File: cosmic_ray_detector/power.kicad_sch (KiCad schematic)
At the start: 16 parts, among them U2 TPS7A30, U3 TPS7A49

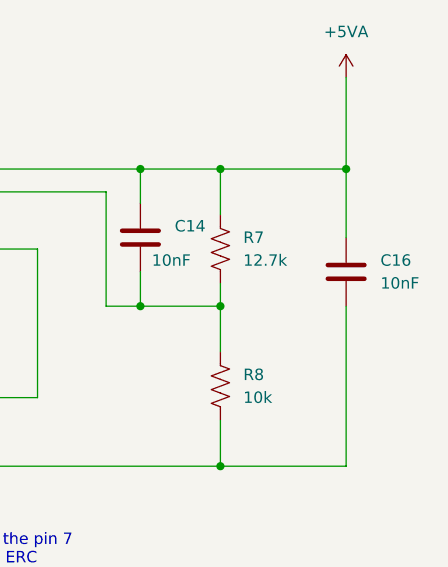
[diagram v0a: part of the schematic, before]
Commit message: change capacitor footprint, place and add zones for +- LDO regs
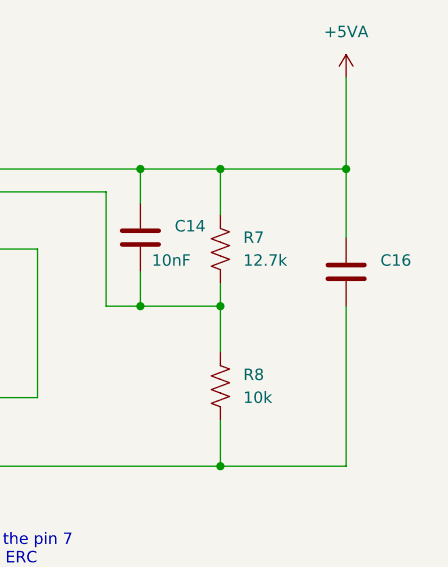
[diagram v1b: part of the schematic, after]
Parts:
- C16: value 10nF -> (none); footprint Capacitor_SMD:C_0402_1005Metric -> (none)
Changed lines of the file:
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@@
       (effects (font (size 1.27 1.27)) (justify left))
     )
-    (property "Value" "10nF" (id 1) (at 180.34 137.1599 0)
+    (property "Value" "" (id 1) (at 180.34 137.1599 0)
       (effects (font (size 1.27 1.27)) (justify left))
     )
-    (property "Footprint" "Capacitor_SMD:C_0402_1005Metric" (id 2) (at 177.4952 139.7 0)
+    (property "Footprint" "" (id 2) (at 177.4952 139.7 0)
       (effects (font (size 1.27 1.27)) hide)
     )

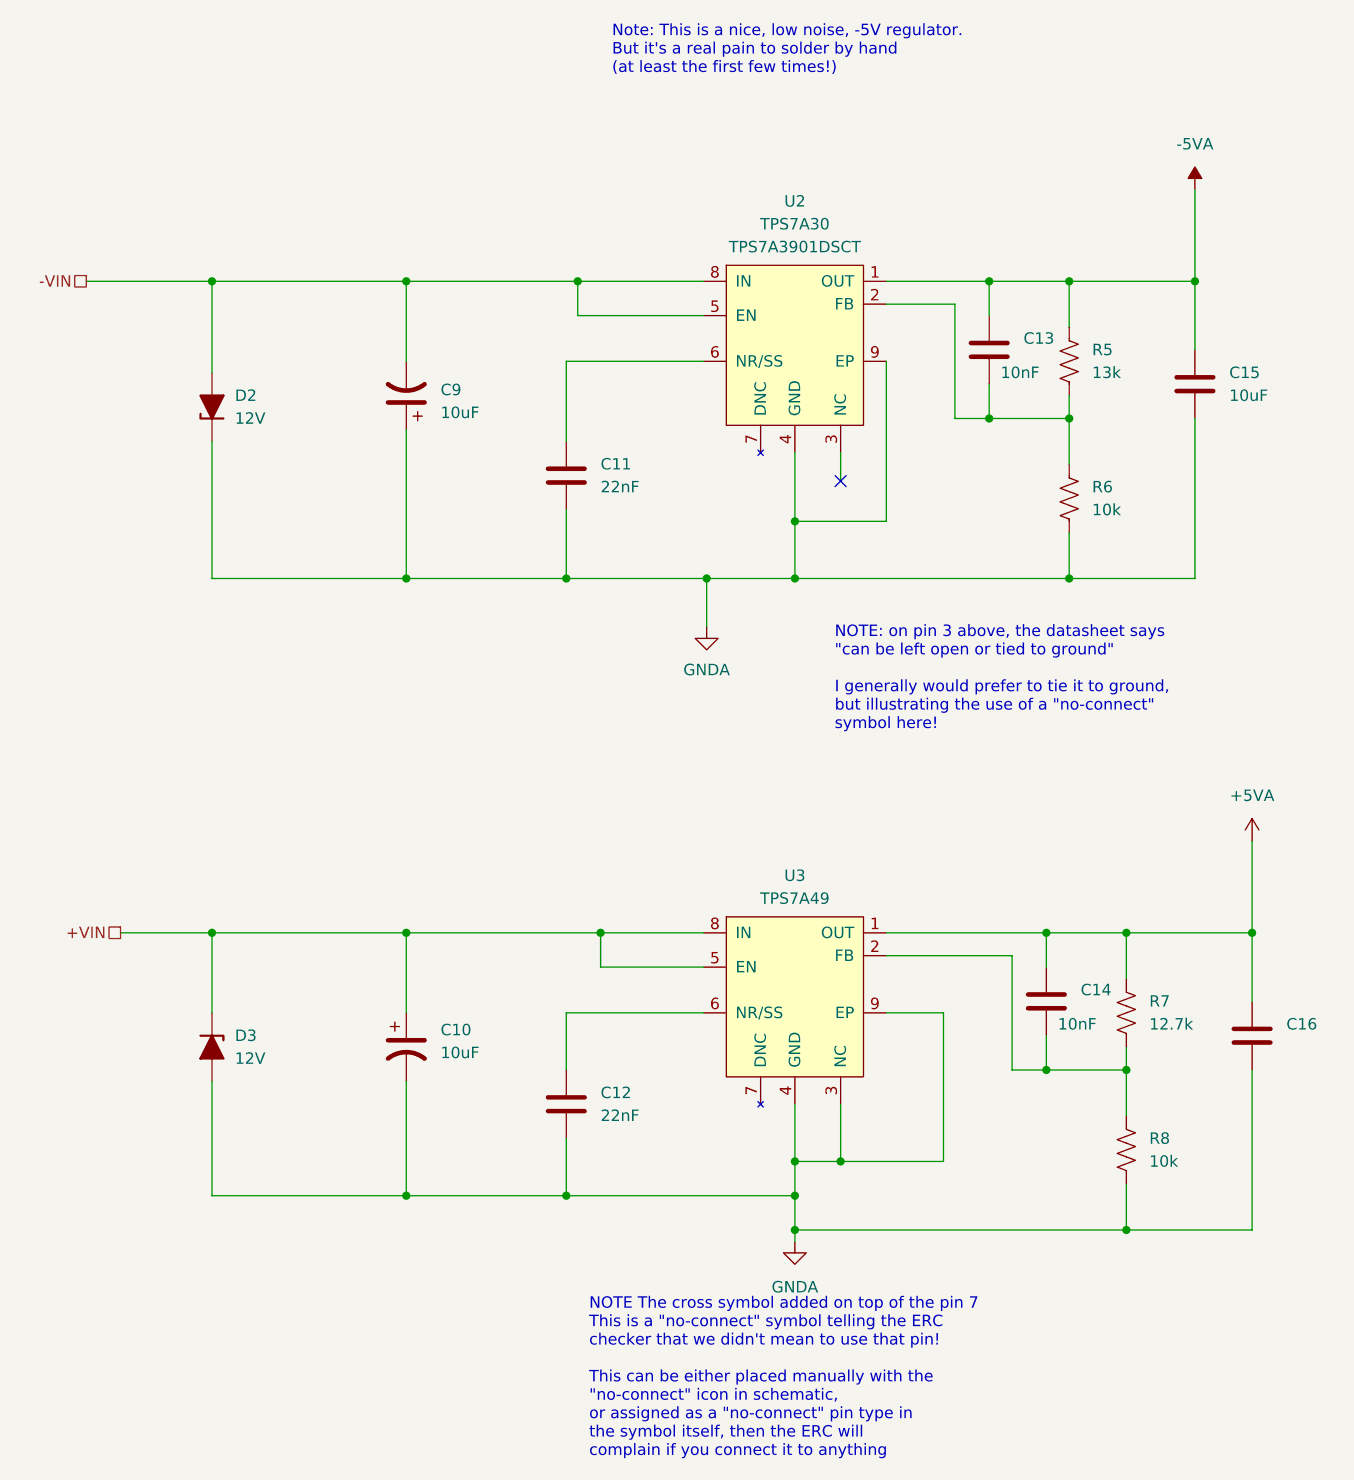
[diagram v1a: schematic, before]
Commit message: changed a couple more caps
all components reasonably grouped, almost placed
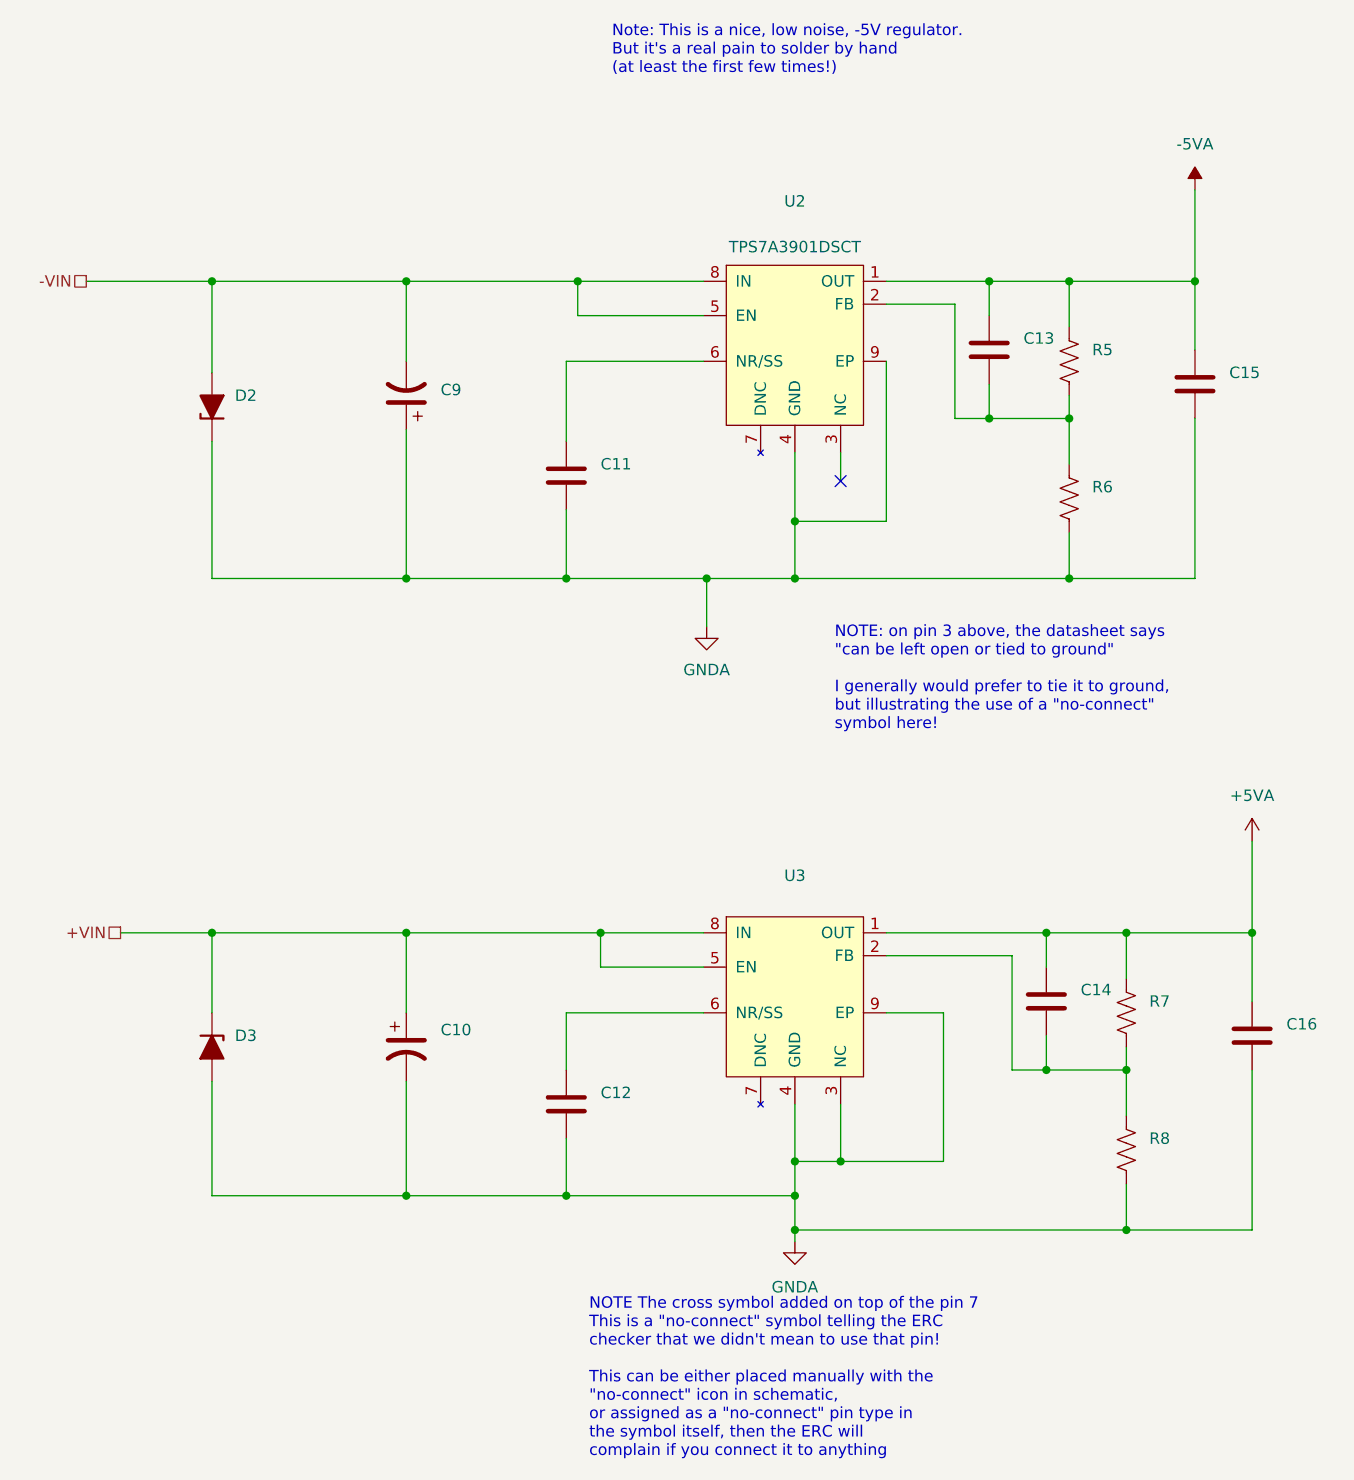
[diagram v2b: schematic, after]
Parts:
- C10, C15, C9: value 10uF -> (none); footprint cosmic_ray_detector_lib:MAL215375109E3 -> (none)
- C11, C12: value 22nF -> (none); footprint Capacitor_SMD:C_0402_1005Metric -> (none)
- C13, C14: value 10nF -> (none); footprint Capacitor_SMD:C_0402_1005Metric -> (none)
- D2, D3: value 12V -> (none); footprint Diode_SMD:D_SOD-123 -> (none)
- R5: value 13k -> (none); footprint Resistor_SMD:R_0402_1005Metric -> (none)
- R6, R8: value 10k -> (none); footprint Resistor_SMD:R_0402_1005Metric -> (none)
- R7: value 12.7k -> (none); footprint Resistor_SMD:R_0402_1005Metric -> (none)
- U2: value TPS7A30 -> (none); footprint cosmic_ray_detector_lib:MSOP-8-1EP_3x3mm_P0.65mm_EP1.73x1.85mm_ThermalVias -> (none)
- U3: value TPS7A49 -> (none); footprint cosmic_ray_detector_lib:MSOP-8-1EP_3x3mm_P0.65mm_EP1.73x1.85mm_ThermalVias -> (none)
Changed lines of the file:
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@@
       (effects (font (size 1.27 1.27)) (justify left))
     )
-    (property "Value" "10k" (id 1) (at 165.1 149.8599 0)
-      (effects (font (size 1.27 1.27)) (justify left))
-    )
-    (property "Footprint" "Resistor_SMD:R_0402_1005Metric" (id 2) (at 163.576 148.844 90)
+    (property "Value" "" (id 1) (at 165.1 149.8599 0)
+      (effects (font (size 1.27 1.27)) (justify left))
+    )
+    (property "Footprint" "" (id 2) (at 163.576 148.844 90)
       (effects (font (size 1.27 1.27)) hide)
     )
@@
       (effects (font (size 1.27 1.27)) (justify left))
     )
-    (property "Value" "12.7k" (id 1) (at 165.1 134.6199 0)
-      (effects (font (size 1.27 1.27)) (justify left))
-    )
-    (property "Footprint" "Resistor_SMD:R_0402_1005Metric" (id 2) (at 163.576 133.604 90)
+    (property "Value" "" (id 1) (at 165.1 134.6199 0)
+      (effects (font (size 1.27 1.27)) (justify left))
+    )
+    (property "Footprint" "" (id 2) (at 163.576 133.604 90)
       (effects (font (size 1.27 1.27)) hide)
     )
@@
       (effects (font (size 1.27 1.27)) (justify left))
     )
-    (property "Value" "10uF" (id 1) (at 86.36 137.7949 0)
-      (effects (font (size 1.27 1.27)) (justify left))
-    )
-    (property "Footprint" "cosmic_ray_detector_lib:MAL215375109E3" (id 2) (at 82.55 137.16 0)
+    (property "Value" "" (id 1) (at 86.36 137.7949 0)
+      (effects (font (size 1.27 1.27)) (justify left))
+    )
+    (property "Footprint" "" (id 2) (at 82.55 137.16 0)
       (effects (font (size 1.27 1.27)) hide)
     )
@@
       (effects (font (size 1.27 1.27)) (justify left))
     )
-    (property "Value" "13k" (id 1) (at 158.75 62.2299 0)
-      (effects (font (size 1.27 1.27)) (justify left))
-    )
-    (property "Footprint" "Resistor_SMD:R_0402_1005Metric" (id 2) (at 157.226 61.214 90)
+    (property "Value" "" (id 1) (at 158.75 62.2299 0)
+      (effects (font (size 1.27 1.27)) (justify left))
+    )
+    (property "Footprint" "" (id 2) (at 157.226 61.214 90)
       (effects (font (size 1.27 1.27)) hide)
     )
@@
       (effects (font (size 1.27 1.27)) (justify left))
     )
-    (property "Value" "10k" (id 1) (at 158.75 77.4699 0)
-      (effects (font (size 1.27 1.27)) (justify left))
-    )
-    (property "Footprint" "Resistor_SMD:R_0402_1005Metric" (id 2) (at 157.226 76.454 90)
+    (property "Value" "" (id 1) (at 158.75 77.4699 0)
+      (effects (font (size 1.27 1.27)) (justify left))
+    )
+    (property "Footprint" "" (id 2) (at 157.226 76.454 90)
       (effects (font (size 1.27 1.27)) hide)
     )
@@
       (effects (font (size 1.27 1.27)) (justify left))
     )
-    (property "Value" "10nF" (id 1) (at 154.94 134.62 0)
-      (effects (font (size 1.27 1.27)) (justify left))
-    )
-    (property "Footprint" "Capacitor_SMD:C_0402_1005Metric" (id 2) (at 154.6352 135.89 0)
+    (property "Value" "" (id 1) (at 154.94 134.62 0)
+      (effects (font (size 1.27 1.27)) (justify left))
+    )
+    (property "Footprint" "" (id 2) (at 154.6352 135.89 0)
       (effects (font (size 1.27 1.27)) hide)
     )
@@
       (effects (font (size 1.27 1.27)) (justify left))
     )
-    (property "Value" "22nF" (id 1) (at 104.14 74.9299 0)
-      (effects (font (size 1.27 1.27)) (justify left))
-    )
-    (property "Footprint" "Capacitor_SMD:C_0402_1005Metric" (id 2) (at 101.2952 77.47 0)
+    (property "Value" "" (id 1) (at 104.14 74.9299 0)
+      (effects (font (size 1.27 1.27)) (justify left))
+    )
+    (property "Footprint" "" (id 2) (at 101.2952 77.47 0)
       (effects (font (size 1.27 1.27)) hide)
     )
@@
       (effects (font (size 1.27 1.27)) (justify left))
     )
-    (property "Value" "12V" (id 1) (at 63.5 138.4299 90)
-      (effects (font (size 1.27 1.27)) (justify left))
-    )
-    (property "Footprint" "Diode_SMD:D_SOD-123" (id 2) (at 60.96 137.16 0)
+    (property "Value" "" (id 1) (at 63.5 138.4299 90)
+      (effects (font (size 1.27 1.27)) (justify left))
+    )
+    (property "Footprint" "" (id 2) (at 60.96 137.16 0)
       (effects (font (size 1.27 1.27)) hide)
     )
@@
     (in_bom yes) (on_board yes) (fields_autoplaced)
     (property "Reference" "U2" (id 0) (at 125.73 43.18 0))
-    (property "Value" "TPS7A30" (id 1) (at 125.73 45.72 0))
-    (property "Footprint" "cosmic_ray_detector_lib:MSOP-8-1EP_3x3mm_P0.65mm_EP1.73x1.85mm_ThermalVias" (id 2) (at 125.73 54.61 0)
+    (property "Value" "" (id 1) (at 125.73 45.72 0))
+    (property "Footprint" "" (id 2) (at 125.73 54.61 0)
       (effects (font (size 1.27 1.27)) hide)
     )
@@
       (effects (font (size 1.27 1.27)) (justify left))
     )
-    (property "Value" "10uF" (id 1) (at 173.99 64.7699 0)
-      (effects (font (size 1.27 1.27)) (justify left))
-    )
-    (property "Footprint" "cosmic_ray_detector_lib:MAL215375109E3" (id 2) (at 171.1452 67.31 0)
+    (property "Value" "" (id 1) (at 173.99 64.7699 0)
+      (effects (font (size 1.27 1.27)) (justify left))
+    )
+    (property "Footprint" "" (id 2) (at 171.1452 67.31 0)
       (effects (font (size 1.27 1.27)) hide)
     )
@@
     (in_bom yes) (on_board yes) (fields_autoplaced)
     (property "Reference" "U3" (id 0) (at 125.73 118.11 0))
-    (property "Value" "TPS7A49" (id 1) (at 125.73 120.65 0))
-    (property "Footprint" "cosmic_ray_detector_lib:MSOP-8-1EP_3x3mm_P0.65mm_EP1.73x1.85mm_ThermalVias" (id 2) (at 125.73 127 0)
+    (property "Value" "" (id 1) (at 125.73 120.65 0))
+    (property "Footprint" "" (id 2) (at 125.73 127 0)
       (effects (font (size 1.27 1.27)) hide)
     )
@@
       (effects (font (size 1.27 1.27)) (justify left))
     )
-    (property "Value" "22nF" (id 1) (at 104.14 144.7799 0)
-      (effects (font (size 1.27 1.27)) (justify left))
-    )
-    (property "Footprint" "Capacitor_SMD:C_0402_1005Metric" (id 2) (at 101.2952 147.32 0)
+    (property "Value" "" (id 1) (at 104.14 144.7799 0)
+      (effects (font (size 1.27 1.27)) (justify left))
+    )
+    (property "Footprint" "" (id 2) (at 101.2952 147.32 0)
       (effects (font (size 1.27 1.27)) hide)
     )
@@
       (effects (font (size 1.27 1.27)) (justify right))
     )
-    (property "Value" "12V" (id 1) (at 63.5 67.3099 90)
+    (property "Value" "" (id 1) (at 63.5 67.3099 90)
       (effects (font (size 1.27 1.27)) (justify right))
     )
-    (property "Footprint" "Diode_SMD:D_SOD-123" (id 2) (at 60.96 66.04 0)
+    (property "Footprint" "" (id 2) (at 60.96 66.04 0)
       (effects (font (size 1.27 1.27)) hide)
     )
@@
       (effects (font (size 1.27 1.27)) (justify left))
     )
-    (property "Value" "10nF" (id 1) (at 148.59 62.23 0)
-      (effects (font (size 1.27 1.27)) (justify left))
-    )
-    (property "Footprint" "Capacitor_SMD:C_0402_1005Metric" (id 2) (at 148.2852 63.5 0)
+    (property "Value" "" (id 1) (at 148.59 62.23 0)
+      (effects (font (size 1.27 1.27)) (justify left))
+    )
+    (property "Footprint" "" (id 2) (at 148.2852 63.5 0)
       (effects (font (size 1.27 1.27)) hide)
     )
@@
       (effects (font (size 1.27 1.27)) (justify right))
     )
-    (property "Value" "10uF" (id 1) (at 86.36 66.6749 0)
+    (property "Value" "" (id 1) (at 86.36 66.6749 0)
       (effects (font (size 1.27 1.27)) (justify right))
     )
-    (property "Footprint" "cosmic_ray_detector_lib:MAL215375109E3" (id 2) (at 82.55 64.77 0)
-      (effects (font (size 1.27 1.27)) hide)
-    )
+    (property "Footprint" "" (id 2) (at 82.55 64.77 0)
+      (effects (font (size 1.27 1.27)) hide)
+    )
